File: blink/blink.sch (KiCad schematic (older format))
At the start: 5 parts

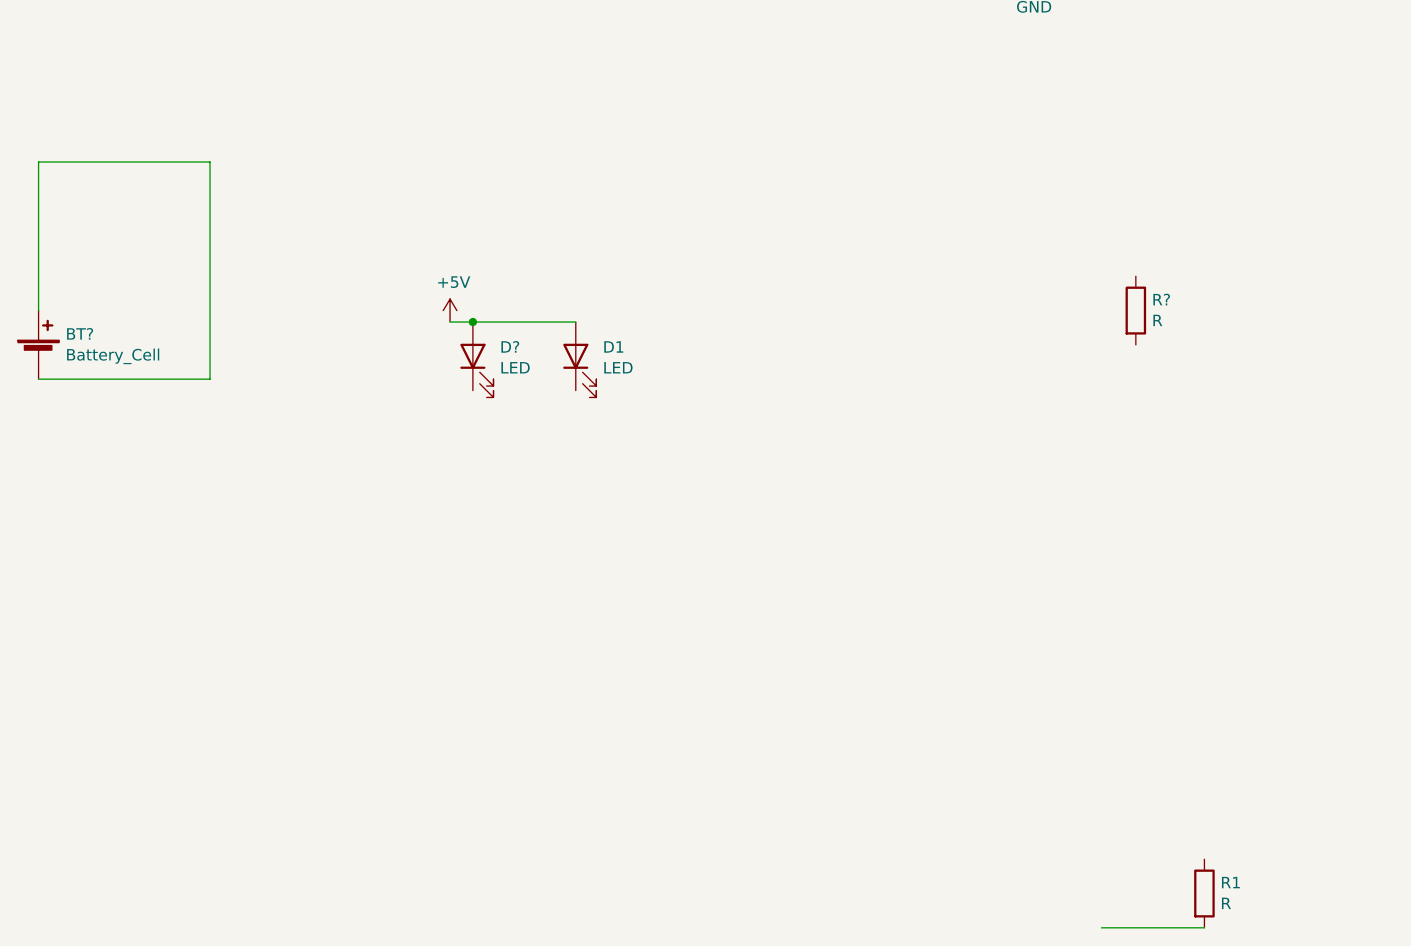
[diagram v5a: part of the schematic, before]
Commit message: Added super capacitor
:100:
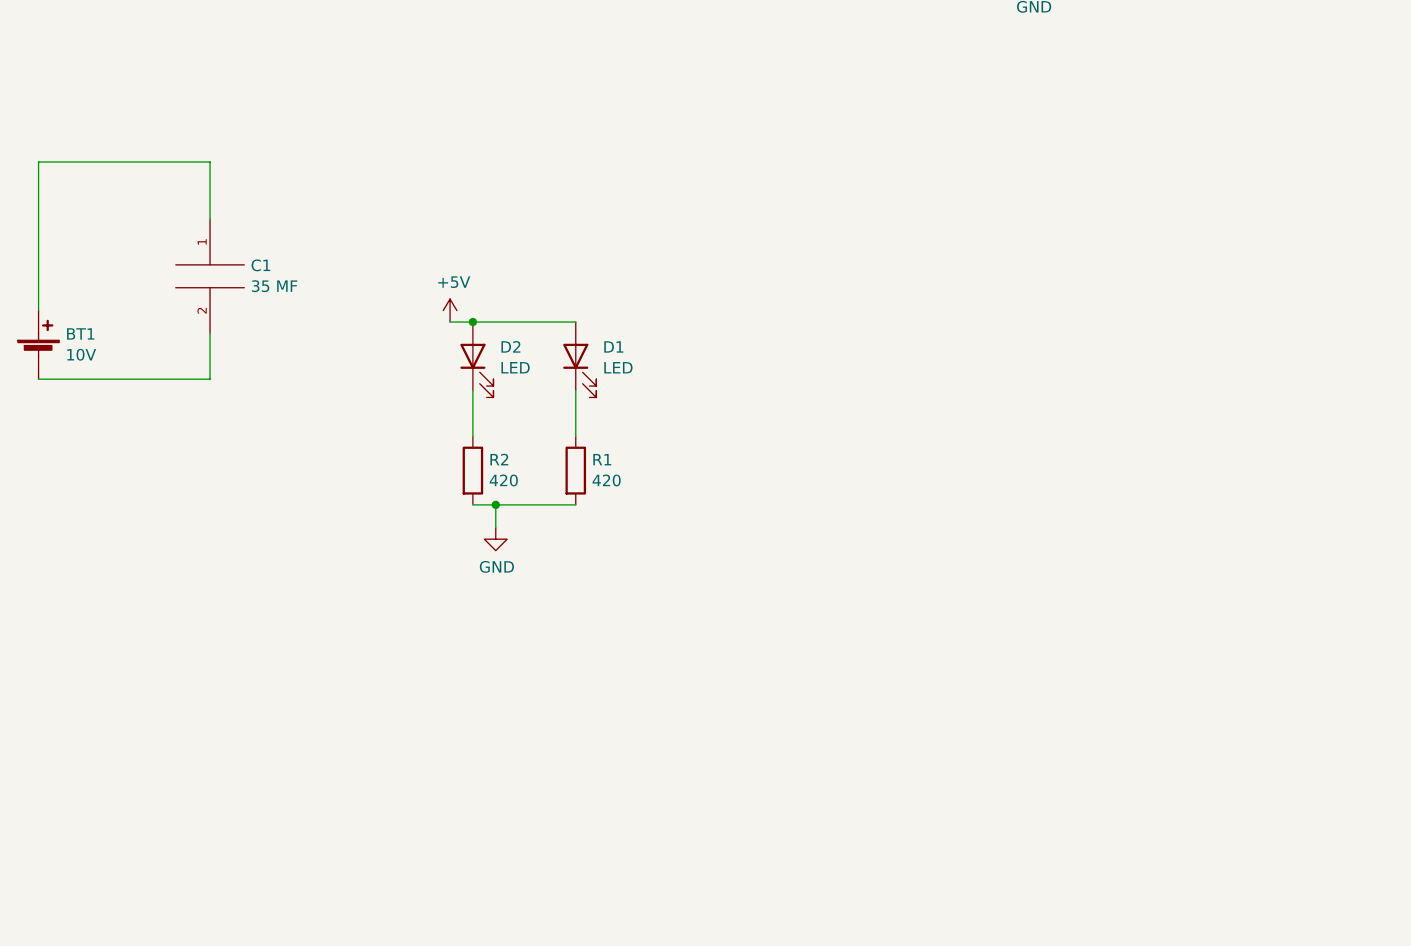
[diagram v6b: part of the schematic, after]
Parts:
- added C1: 35 MF, symbol pspice:C
- BT1: renamed from BT?; value Battery_Cell -> 10V
- R1: value R -> 420
- R2: renamed from R?; value R -> 420
- gave numbers to parts that had none: 1
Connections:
- wire segments 11 -> 16
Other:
- moved on the sheet: R1, R2
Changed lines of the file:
@@
 L Device:R R1
 U 1 1 5FBDBA5D
-P 8050 4750
-F 0 "R1" H 8120 4796 50  0000 L CNN
-F 1 "R" H 8120 4705 50  0000 L CNN
-F 2 "Resistor_THT:R_Axial_DIN0204_L3.6mm_D1.6mm_P1.90mm_Vertical" V 7980 4750 50  0001 C CNN
-F 3 "~" H 8050 4750 50  0001 C CNN
-	1    8050 4750
+P 5300 2900
+F 0 "R1" H 5370 2946 50  0000 L CNN
+F 1 "420" H 5370 2855 50  0000 L CNN
+F 2 "Resistor_THT:R_Axial_DIN0204_L3.6mm_D1.6mm_P1.90mm_Vertical" V 5230 2900 50  0001 C CNN
+F 3 "~" H 5300 2900 50  0001 C CNN
+	1    5300 2900
 	1    0    0    -1
 $EndComp
@@
 $EndComp
 $Comp
-L Device:LED D?
+L Device:LED D2
 U 1 1 5FBDCB34
 P 4850 2400
-F 0 "D?" V 4889 2282 50  0000 R CNN
+F 0 "D2" V 4889 2282 50  0000 R CNN
 F 1 "LED" V 4798 2282 50  0000 R CNN
 F 2 "" H 4850 2400 50  0001 C CNN
@@
 	7300 600  7400 600
 $Comp
-L Device:R R?
+L Device:R R2
 U 1 1 5FBDD47C
-P 7750 2200
-F 0 "R?" H 7820 2246 50  0000 L CNN
-F 1 "R" H 7820 2155 50  0000 L CNN
-F 2 "" V 7680 2200 50  0001 C CNN
-F 3 "~" H 7750 2200 50  0001 C CNN
-	1    7750 2200
+P 4850 2900
+F 0 "R2" H 4920 2946 50  0000 L CNN
+F 1 "420" H 4920 2855 50  0000 L CNN
+F 2 "" V 4780 2900 50  0001 C CNN
+F 3 "~" H 4850 2900 50  0001 C CNN
+	1    4850 2900
 	1    0    0    -1
 $EndComp
 Wire Wire Line
-	7600 4900 8050 4900
+	4850 3050 4950 3050
 $Comp
-L Device:Battery_Cell BT?
+L Device:Battery_Cell BT1
 U 1 1 5FBDEFE5
 P 2950 2400
-F 0 "BT?" H 3068 2496 50  0000 L CNN
-F 1 "Battery_Cell" H 3068 2405 50  0000 L CNN
+F 0 "BT1" H 3068 2496 50  0000 L CNN
+F 1 "10V" H 3068 2405 50  0000 L CNN
 F 2 "" V 2950 2460 50  0001 C CNN
 F 3 "~" V 2950 2460 50  0001 C CNN
@@
 	2950 1550 3700 1550
 Wire Wire Line
-	3700 1550 3700 2500
+	3700 2500 2950 2500
 Wire Wire Line
-	3700 2500 2950 2500
+	4850 2550 4850 2750
+Wire Wire Line
+	5300 2750 5300 2550
+$Comp
+L pspice:C C1
+U 1 1 5FBDEBC5
+P 3700 2050
+F 0 "C1" H 3878 2096 50  0000 L CNN
+F 1 "35 MF" H 3878 2005 50  0000 L CNN
+F 2 "" H 3700 2050 50  0001 C CNN
+F 3 "~" H 3700 2050 50  0001 C CNN
+	1    3700 2050
+	1    0    0    -1
+$EndComp
+Wire Wire Line
+	3700 1550 3700 1800
+Wire Wire Line
+	3700 2300 3700 2500
+$Comp
+L power:GND #PWR0103
+U 1 1 5FBDFD72
+P 4950 3150
+F 0 "#PWR0103" H 4950 2900 50  0001 C CNN
+F 1 "GND" H 4955 2977 50  0000 C CNN
+F 2 "" H 4950 3150 50  0001 C CNN
+F 3 "" H 4950 3150 50  0001 C CNN
+	1    4950 3150
+	1    0    0    -1
+$EndComp
+Wire Wire Line
+	4950 3150 4950 3050
+Connection ~ 4950 3050
+Wire Wire Line
+	4950 3050 5300 3050
 $EndSCHEMATC

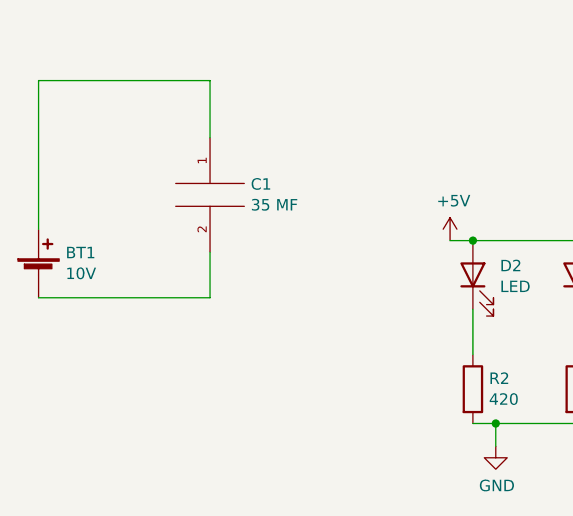
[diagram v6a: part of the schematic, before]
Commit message: added 1V source
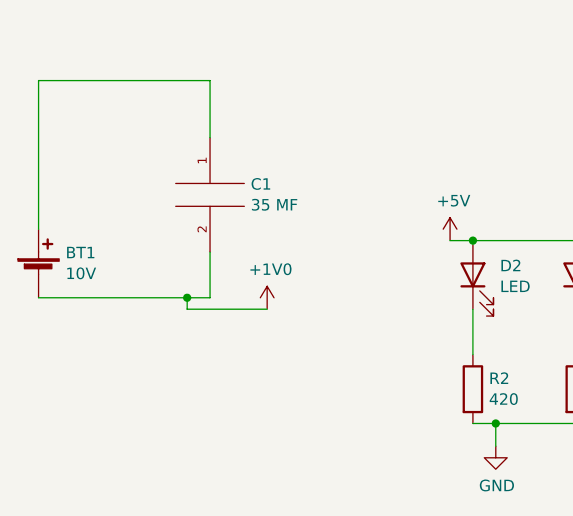
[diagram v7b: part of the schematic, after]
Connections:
- net labels added: +1V0
- wire segments 16 -> 19
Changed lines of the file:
@@
 	2950 1550 3700 1550
 Wire Wire Line
-	3700 2500 2950 2500
+	3700 2500 3600 2500
 Wire Wire Line
 	4850 2550 4850 2750
@@
 Wire Wire Line
 	4950 3050 5300 3050
+$Comp
+L power:+1V0 #PWR?
+U 1 1 5FC59A04
+P 3950 2550
+F 0 "#PWR?" H 3950 2400 50  0001 C CNN
+F 1 "+1V0" H 3965 2723 50  0000 C CNN
+F 2 "" H 3950 2550 50  0001 C CNN
+F 3 "" H 3950 2550 50  0001 C CNN
+	1    3950 2550
+	1    0    0    -1
+$EndComp
+Wire Wire Line
+	3950 2550 3600 2550
+Wire Wire Line
+	3600 2550 3600 2500
+Connection ~ 3600 2500
+Wire Wire Line
+	3600 2500 2950 2500
 $EndSCHEMATC

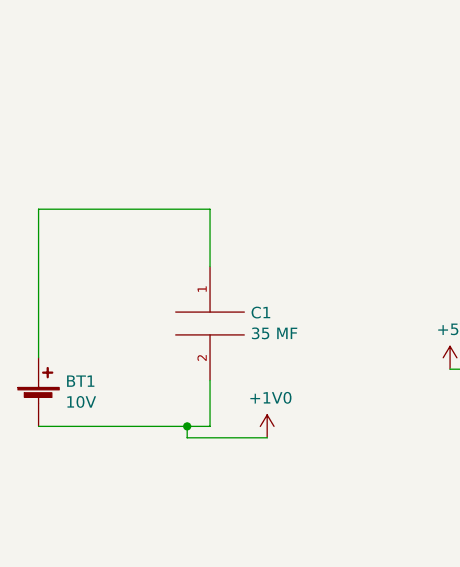
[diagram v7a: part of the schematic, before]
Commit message: Update blink.sch
Added a resistor
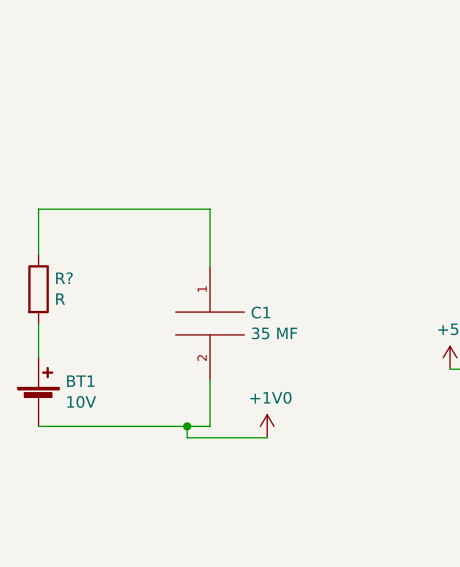
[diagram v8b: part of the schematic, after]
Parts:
- added R?: R, symbol Device:R
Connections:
- wire segments 19 -> 20
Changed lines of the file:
@@
 	16000 -1800 16000 -4200
 Wire Wire Line
-	2950 2200 2950 1550
+	2950 2200 2950 2050
 Wire Wire Line
 	2950 1550 3700 1550
@@
 Wire Wire Line
 	3600 2500 2950 2500
+$Comp
+L Device:R R?
+U 1 1 5FC5E211
+P 2950 1900
+F 0 "R?" H 3020 1946 50  0000 L CNN
+F 1 "R" H 3020 1855 50  0000 L CNN
+F 2 "" V 2880 1900 50  0001 C CNN
+F 3 "~" H 2950 1900 50  0001 C CNN
+	1    2950 1900
+	1    0    0    -1
+$EndComp
+Wire Wire Line
+	2950 1750 2950 1550
 $EndSCHEMATC
